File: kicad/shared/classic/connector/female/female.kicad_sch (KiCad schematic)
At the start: 0 parts

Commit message: feat: Added connector schematics and fixed some other connectors in other schematics
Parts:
- added J1: XLR5, symbol Connector_Audio:XLR5
- added J2: Conn_01x05, symbol Connector_Generic:Conn_01x05
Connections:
- new net: J1.1 (P1), J2.1 (Pin_1)
- new net: J1.2 (P2), J2.2 (Pin_2)
- new net: J1.3 (P3), J2.3 (Pin_3)
- new net: J1.4 (P3), J2.4 (Pin_4)
- new net: J1.5 (P5), J2.5 (Pin_5)

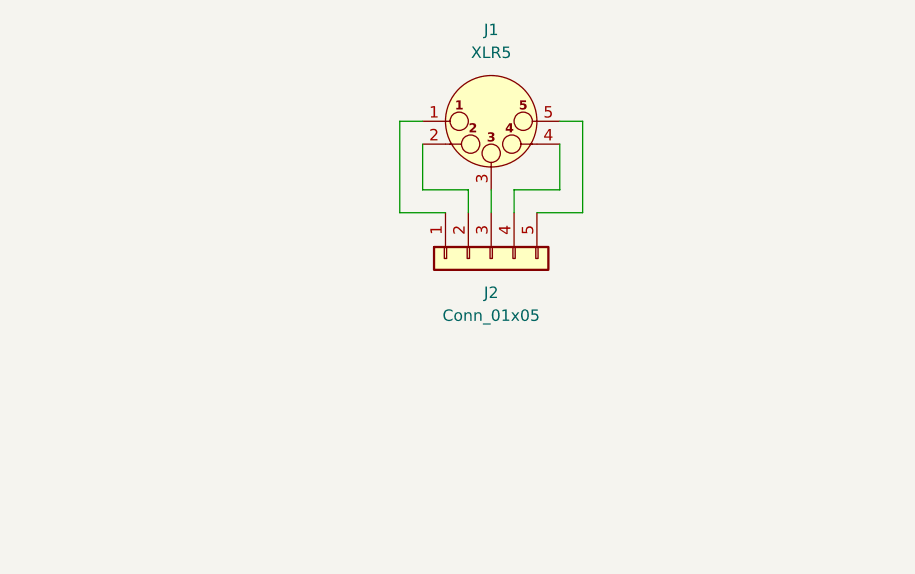
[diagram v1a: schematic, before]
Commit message: Added ESD protection for USB/RS485, not for serial lines yet; harmonised XLR pin numbers between boards
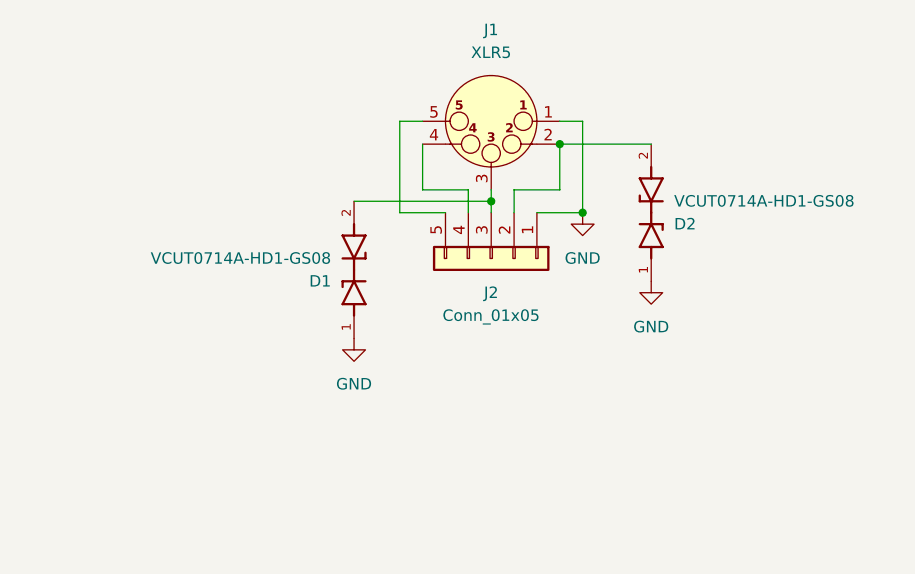
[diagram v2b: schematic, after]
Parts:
- added D1, D2: VCUT0714A-HD1-GS08, VCUT0714A-HD1-GS08:DIO_VCUT0714A-HD1-GS08, symbol VCUT0714A-HD1-GS08:VCUT0714A-HD1-GS08
- J2: footprint (none) -> Connector_JST:JST_XA_B05B-XASK-1-A_1x05_P2.50mm_Vertical
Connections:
- net GND: now reaches J1.1 (P1), J2.1 (Pin_1)
- net GND: now also D1.1, D2.1
- net at J1.2 (P2), J2.2 (Pin_2): now also D2.2
- net at J1.3 (P3), J2.3 (Pin_3): now also D1.2
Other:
- moved on the sheet: J2

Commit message: Added some stuff for ESD protection on the serial lines; redid the STM32 programming pins
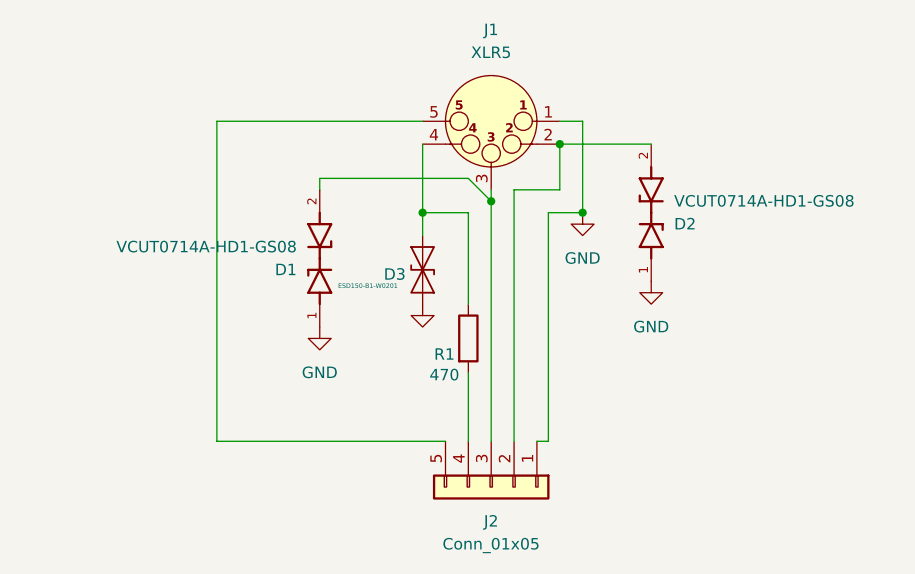
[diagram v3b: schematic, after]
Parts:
- added D3: ESD150-B1-W0201, Diode_SMD:Infineon_SG-WLL-2-3_0.58x0.28_P0.36mm, symbol Diode:ESD131-B1-W0201
- added R1: 470, symbol Device:R
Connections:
- net GND: now also D3.1 (A1)
- net at J1.4 (P3): now also D3.2 (A2), R1.1; no longer J2.4 (Pin_4)
- new net: J2.4 (Pin_4), R1.2
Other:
- moved on the sheet: D1, J2

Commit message: feat: Should be able to footprint and route some prototype boards to see if I'm not totally off-base here
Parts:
- added D4: ESD150-B1-W0201, Diode_SMD:Infineon_SG-WLL-2-3_0.58x0.28_P0.36mm, symbol Diode:ESD131-B1-W0201
- added R2: 7.5, symbol Device:R
- R1: value 470 -> 240
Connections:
- net GND: now also D4.1 (A1)
- net at J1.5 (P5): now also D4.2 (A2), R2.1; no longer J2.5 (Pin_5)
- new net: J2.5 (Pin_5), R2.2
